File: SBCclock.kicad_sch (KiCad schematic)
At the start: 20 parts, among them J1 Conn_01x07, J2 Conn_01x07, U1 74HCT14, U2 74HCT163, U3 74HCT112, U5 74HCT153, Y1 25.175MHz

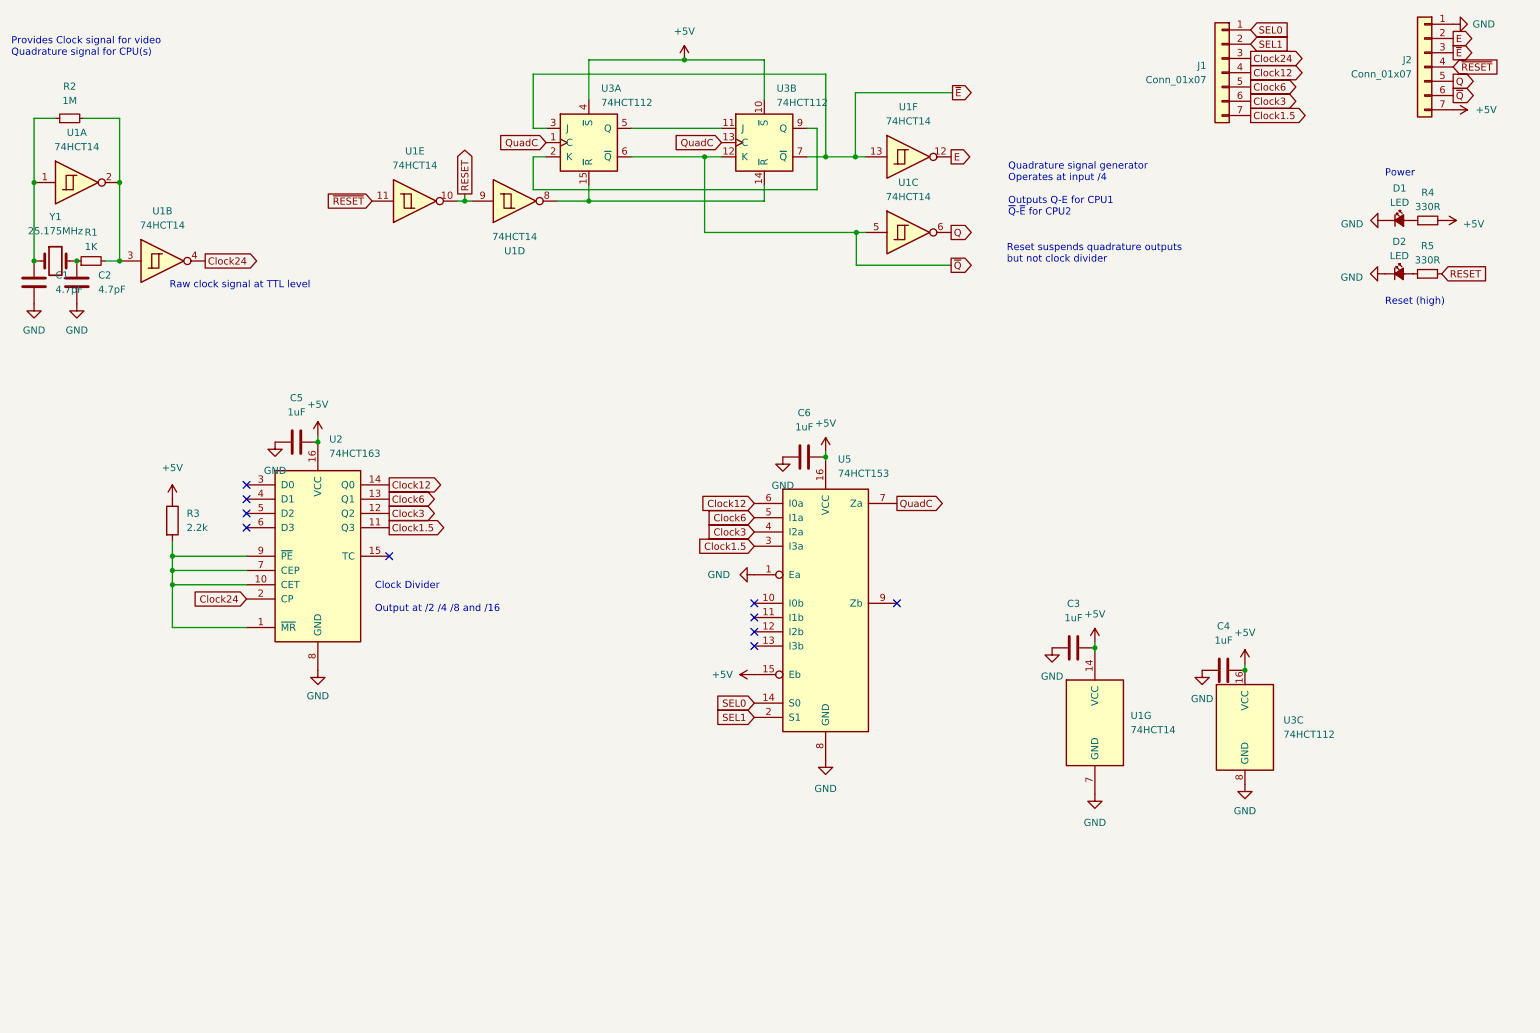
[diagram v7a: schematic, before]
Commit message: reinforce clock outputs
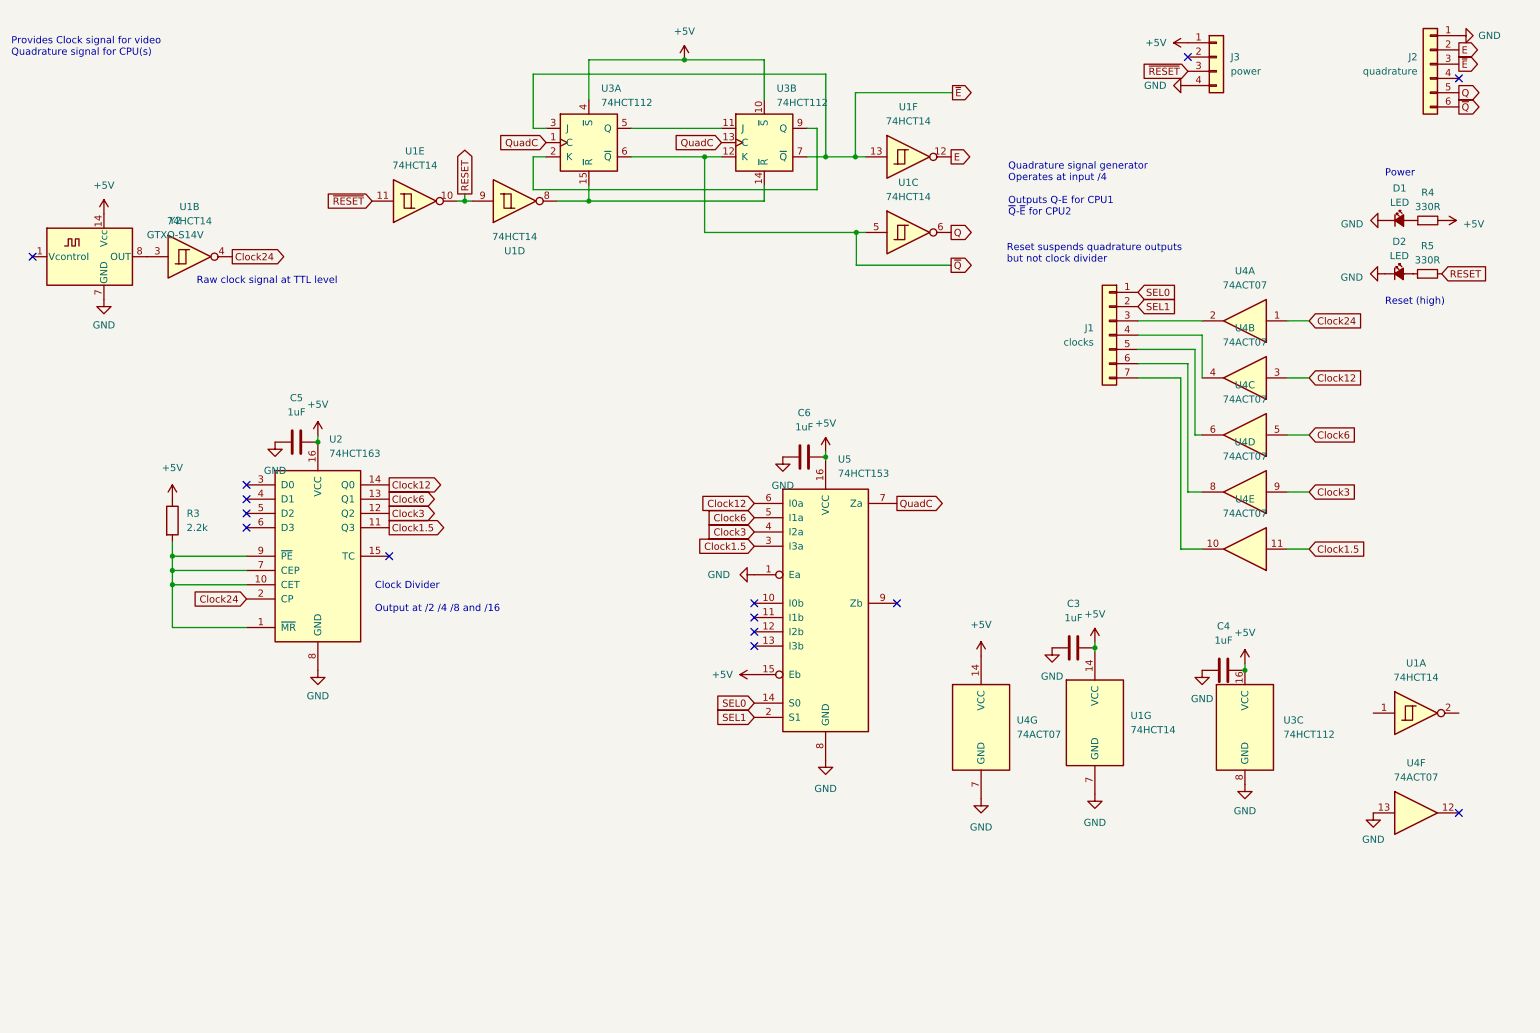
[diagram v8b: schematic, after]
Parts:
- removed C1, C2: 4.7pF, Capacitor_SMD:C_0805_2012Metric_Pad1.18x1.45mm_HandSolder, symbol Device:C
- removed R1: 1K, Resistor_SMD:R_0805_2012Metric_Pad1.20x1.40mm_HandSolder, symbol Device:R_Small
- removed R2: 1M, Resistor_SMD:R_0805_2012Metric_Pad1.20x1.40mm_HandSolder, symbol Device:R_Small
- removed Y1: 25.175MHz, Crystal:Crystal_SMD_HC49-SD, symbol Device:Crystal
- added J3: power, Connector_PinHeader_2.54mm:PinHeader_1x04_P2.54mm_Vertical, symbol Connector_Generic:Conn_01x04
- added U4: 74ACT07, Package_SO:TSSOP-14_4.4x3.6mm_P0.4mm, symbol 74xx:74LS07
- added Y2: GTXO-S14V, Oscillator:Oscillator_DIP-14, symbol Oscillator:GTXO-S14V
- J1: value Conn_01x07 -> clocks
- J2: value Conn_01x07 -> quadrature; footprint Connector_PinHeader_2.54mm:PinHeader_1x07_P2.54mm_Vertical -> Connector_PinHeader_2.54mm:PinHeader_1x06_P2.54mm_Vertical; symbol Connector_Generic:Conn_01x07 -> Connector_Generic:Conn_01x06
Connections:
- net +5V: now also J3.1 (Pin_1), U4.14 (VCC), Y2.14 (Vcc); no longer J2.7 (Pin_7)
- net Clock1.5: now also U4.11; no longer J1.7 (Pin_7)
- net Clock12: now also U4.3; no longer J1.4 (Pin_4)
- net Clock24: now also U4.1; no longer J1.3 (Pin_3)
- net Clock3: now also U4.9; no longer J1.6 (Pin_6)
- net Clock6: now also U4.5; no longer J1.5 (Pin_5)
- net GND: now also J3.4 (Pin_4), U4.13, U4.7 (GND), Y2.7 (GND)
- net ~{RESET}: now also J3.3 (Pin_3); no longer J2.4 (Pin_4)
- net at U1.2: no longer U1.3
- new net: J1.3 (Pin_3), U4.2
- new net: J1.6 (Pin_6), U4.8
- new net: J1.4 (Pin_4), U4.4
- new net: J1.5 (Pin_5), U4.6
- new net: J1.7 (Pin_7), U4.10
- new net: U1.3, Y2.8 (OUT)
- no-connect marks 10 -> 14
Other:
- moved on the sheet: J1, U1B
